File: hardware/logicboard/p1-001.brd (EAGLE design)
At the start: 47 x 72 mm, 24 parts, among them IC1 74LS07N

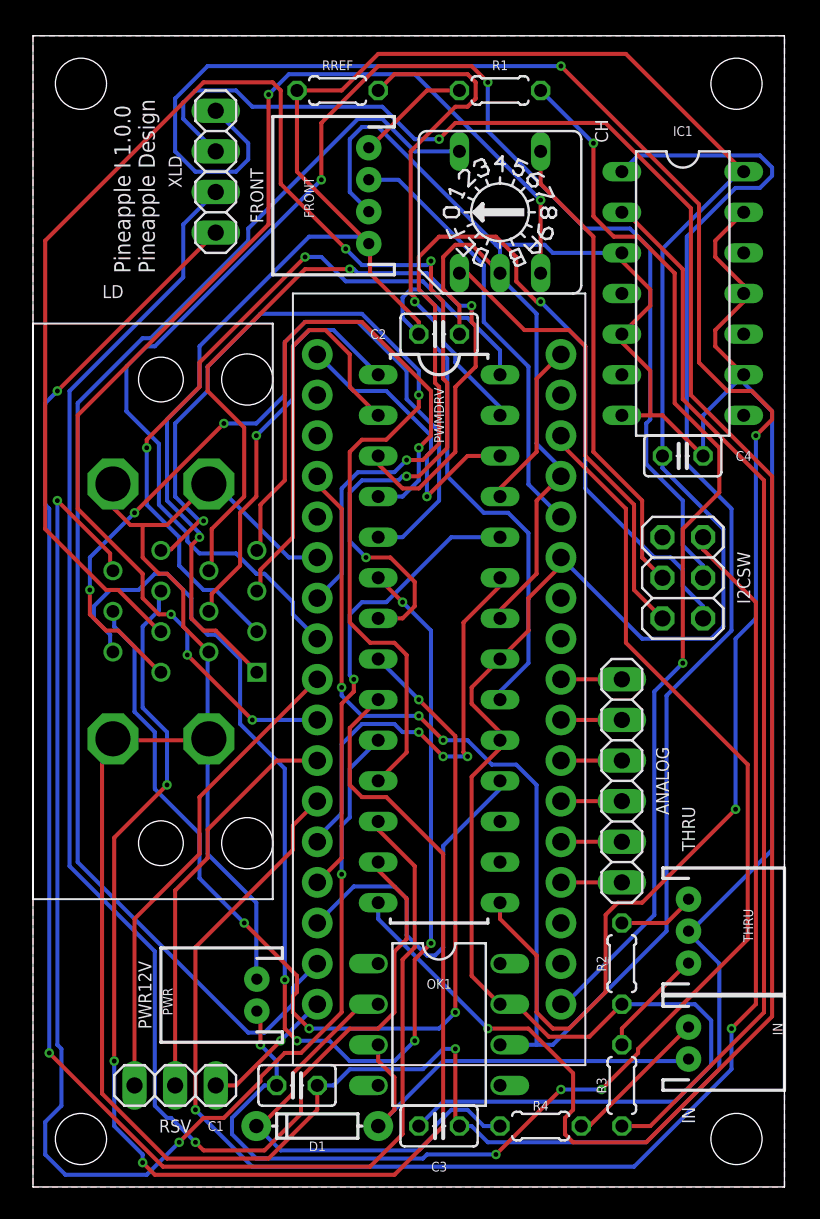
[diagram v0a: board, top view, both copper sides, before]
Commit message: Added MKR compatible I2C connector.
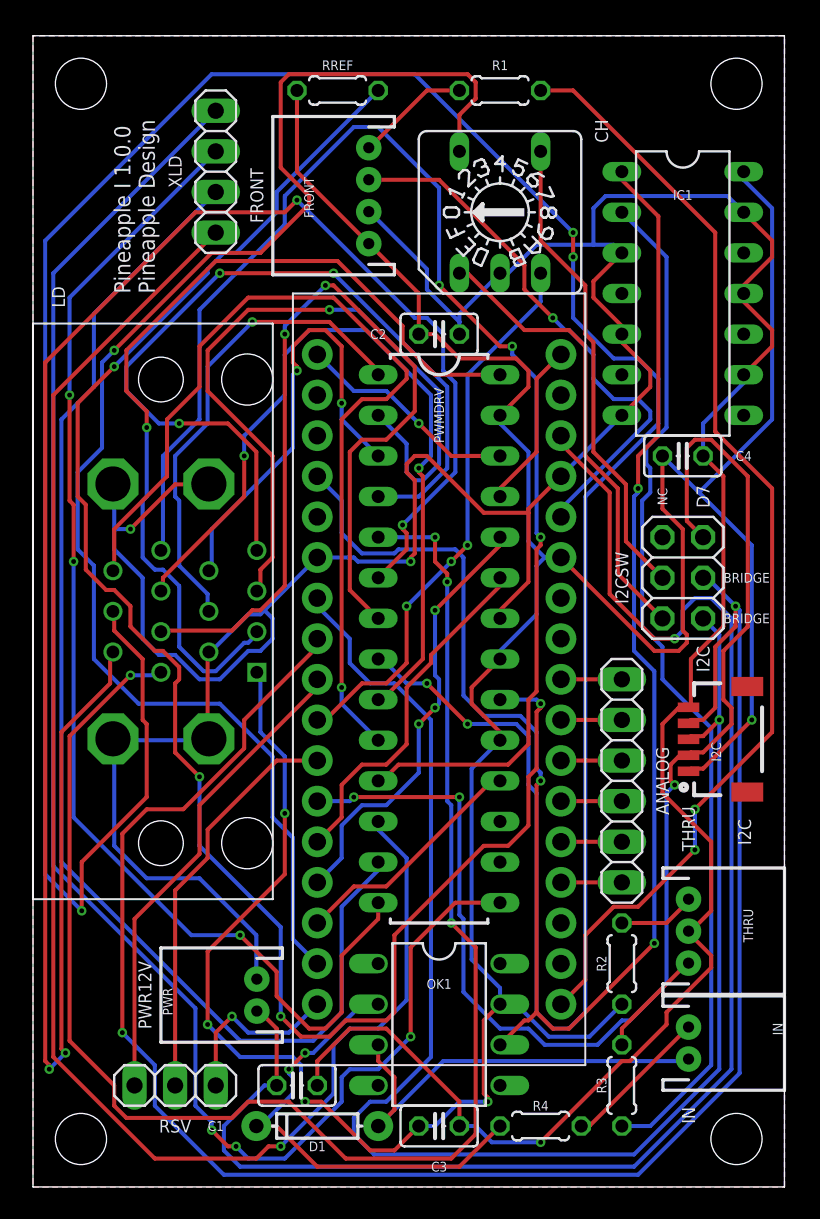
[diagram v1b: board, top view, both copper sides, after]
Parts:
- added I2C: (no value), SparkFun-Connectors:1X05_1MM_RA
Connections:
- net N$11 renamed SW1
- net N$12 renamed SW2
- net N$14 renamed SW4
- net N$15 renamed SW8
- removed net N$10: I2CSW.3, U$1.P$10
- removed net N$13: I2CSW.5, U$1.P$6
- removed net N$9: I2CSW.1, U$1.P$11
- new net D7: I2C.2, I2CSW.5, U$1.P$6
- new net SCL: I2C.4, I2CSW.3, U$1.P$10
- new net SDA: I2C.3, I2CSW.1, U$1.P$11
- net GND: now also I2C.5
- net VCC: now also I2C.1
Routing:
- net LD9: track 65.0 -> 192.1 mm, vias 4 -> 5
- net SCL: track 0.00 -> 118.5 mm, vias 0 -> 2
- net SDA: track 0.00 -> 96.6 mm, vias 0 -> 1
- net N$13: track 95.3 -> 0.00 mm, vias 2 -> 0
- net N$10: track 94.9 -> 0.00 mm, vias 2 -> 0
- net D7: track 0.00 -> 83.1 mm, vias 0 -> 3
- net N$9: track 62.3 -> 0.00 mm, vias 2 -> 0
- net IREF: track 52.1 -> 107.1 mm, vias 1 -> 4
- net LD15: track 130.2 -> 76.9 mm, vias 2 -> 3
- net LD6: track 52.3 -> 99.1 mm, vias 3 -> 4
- net SW4: track 78.5 -> 34.9 mm, vias 5 -> 3
- net LD7: track 80.9 -> 122.6 mm, vias 5 -> 4
- net LD8: track 96.1 -> 55.5 mm, vias 4 -> 2
- net LD10: track 90.0 -> 50.3 mm, vias 3 -> 2
- net LD11: track 88.7 -> 59.0 mm, vias 3 -> 1
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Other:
- board text added: "BRIDGE"
- board text added: "D7"
- board text added: "I2C"
- board text added: "NC"

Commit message: Layout.
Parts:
- turned I2CSW to 270 degrees
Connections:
- net SCL: now also I2C.3; no longer I2C.4
- net SDA: now also I2C.4; no longer I2C.3
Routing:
- net LD9: track 192.1 -> 125.7 mm, vias 5 -> 2
- net LD7: track 122.6 -> 57.7 mm, vias 4 -> 3
- net IREF: track 107.1 -> 47.0 mm, vias 4 -> 0
- net LD6: track 99.1 -> 47.7 mm, vias 4 -> 0
- net SCL: track 118.5 -> 72.4 mm, vias 2 -> 4
- net GND: track 248.9 -> 219.1 mm, vias 3 -> 0
- net LD14: track 79.1 -> 52.8 mm, vias 0 -> 2
- net LD16: track 101.6 -> 124.1 mm, vias 3 -> 1
- net LD3: track 46.4 -> 26.8 mm, vias 1 -> 0
- net LD4: track 28.2 -> 47.2 mm, vias 2 -> 5
- net LD1: track 56.2 -> 71.9 mm, vias 1 -> 3
- net VCC: track 206.4 -> 191.3 mm, vias 5 -> 2
- net LD5: track 53.0 -> 39.2 mm, vias 3 -> 5
- net XLAT: track 27.4 -> 38.4 mm, vias 3 -> 1
- net SW2: track 29.8 -> 40.1 mm
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
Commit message: New silk.
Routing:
- net GND: track 219.1 -> 0.00 mm
- net VCC: track 191.3 -> 0.00 mm, vias 2 -> 0
- net LD9: track 125.7 -> 0.00 mm, vias 2 -> 0
- net LD16: track 124.1 -> 0.00 mm, vias 1 -> 0
- net RX: track 111.7 -> 0.00 mm, vias 2 -> 0
- net VDD: track 95.3 -> 0.00 mm, vias 2 -> 0
- net SW8: track 93.7 -> 0.00 mm, vias 1 -> 0
- net LD13: track 93.2 -> 0.00 mm, vias 1 -> 0
- net SDA: track 90.3 -> 0.00 mm, vias 7 -> 0
- net LD15: track 83.7 -> 0.00 mm
- net D7: track 82.1 -> 0.00 mm, vias 3 -> 0
- net LD12: track 78.5 -> 0.00 mm, vias 5 -> 0
- net SCL: track 72.4 -> 0.00 mm, vias 4 -> 0
- net LD1: track 71.9 -> 0.00 mm, vias 3 -> 0
- net LD11: track 67.0 -> 0.00 mm, vias 3 -> 0
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- removed copper zone on layer 1, net GND
- removed copper zone on layer 16, net GND
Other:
- board text added: "USB"

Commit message: new layout.
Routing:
- net GND: track 0.00 -> 260.2 mm, vias 0 -> 1
- net VCC: track 0.00 -> 237.4 mm
- net LD12: track 0.00 -> 163.7 mm, vias 0 -> 1
- net RX: track 0.00 -> 134.9 mm, vias 0 -> 4
- net LD14: track 0.00 -> 113.9 mm, vias 0 -> 2
- net SCL: track 0.00 -> 111.3 mm, vias 0 -> 2
- net LD15: track 0.00 -> 109.3 mm, vias 0 -> 4
- net VDD: track 0.00 -> 97.5 mm, vias 0 -> 2
- net LD13: track 0.00 -> 95.5 mm, vias 0 -> 3
- net LD16: track 0.00 -> 91.8 mm, vias 0 -> 2
- net SW8: track 0.00 -> 91.6 mm, vias 0 -> 2
- net LD7: track 0.00 -> 89.3 mm, vias 0 -> 4
- net IND: track 0.00 -> 74.9 mm, vias 0 -> 2
- net D7: track 0.00 -> 70.3 mm, vias 0 -> 1
- net LD1: track 0.00 -> 69.9 mm, vias 0 -> 4
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- added copper zone on layer 1, net GND
- added copper zone on layer 16, net GND

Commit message: 20 holes.
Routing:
- net LD12: track 163.7 -> 79.5 mm, vias 1 -> 2
- net IREF: track 44.9 -> 109.4 mm
- net RX: track 134.9 -> 87.0 mm
- net SDA: track 56.1 -> 101.1 mm
- net LD13: track 95.5 -> 51.3 mm, vias 3 -> 2
- net VCC: track 237.4 -> 195.9 mm, vias 0 -> 3
- net LD16: track 91.8 -> 128.4 mm, vias 2 -> 1
- net VDD: track 97.5 -> 132.1 mm
- net SCL: track 111.3 -> 137.6 mm
- net SW1: track 24.8 -> 50.1 mm, vias 0 -> 4
- net LD14: track 113.9 -> 138.3 mm, vias 2 -> 0
- net LD8: track 61.9 -> 85.7 mm, vias 3 -> 2
- net GND: track 260.2 -> 237.8 mm, vias 1 -> 2
- net LD15: track 109.3 -> 87.7 mm, vias 4 -> 3
- net SW4: track 55.5 -> 73.3 mm, vias 5 -> 3
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
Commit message: New silk.
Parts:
- added VOUT: (no value), pinhead:1X03
- moved I2CSW 1.27 mm to (41.9, 38.1)
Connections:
- new net 3V: U$1.P$33, VOUT.1, VOUT.2
- net GND: now also VOUT.3
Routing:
- net GND: track 237.8 -> 299.2 mm, vias 2 -> 3
- net LD16: track 128.4 -> 70.2 mm, vias 1 -> 2
- net LD3: track 38.9 -> 77.1 mm, vias 0 -> 9
- net VCC: track 195.9 -> 234.0 mm, vias 3 -> 4
- net RX: track 87.0 -> 125.0 mm, vias 4 -> 3
- net LD14: track 138.3 -> 106.0 mm, vias 0 -> 8
- net LD8: track 85.7 -> 55.8 mm, vias 2 -> 3
- net SCL: track 137.6 -> 107.8 mm, vias 2 -> 3
- net LD12: track 79.5 -> 106.7 mm, vias 2 -> 7
- net 3V: track 0.00 -> 25.7 mm
- net LD4: track 58.5 -> 33.2 mm, vias 1 -> 2
- net LD11: track 64.1 -> 87.0 mm, vias 2 -> 3
- net LD9: track 59.7 -> 82.4 mm, vias 1 -> 7
- net SDA: track 101.1 -> 120.7 mm
- net LD6: track 77.9 -> 58.8 mm, vias 2 -> 5
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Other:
- board text added: "G"
- board text removed: "BRIDGE"

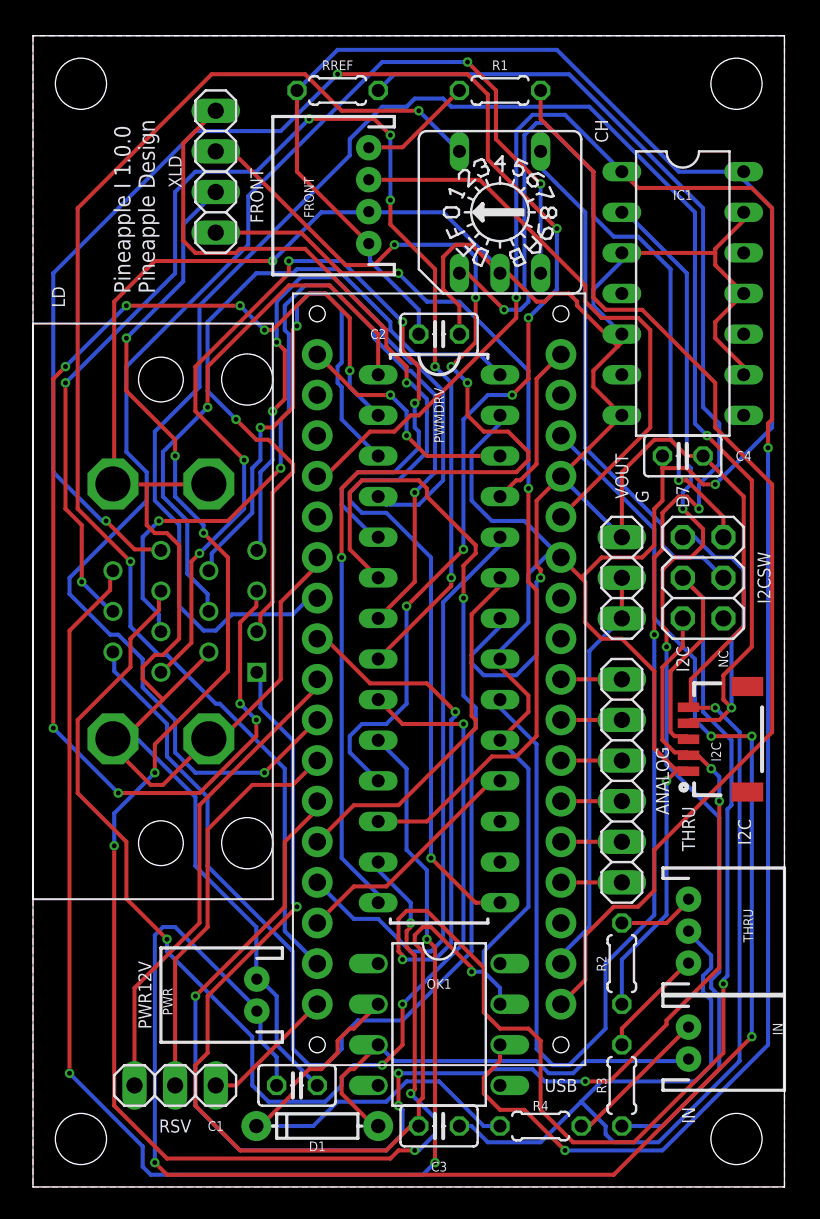
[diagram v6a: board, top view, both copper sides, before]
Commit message: Vcc and Vref terminal.
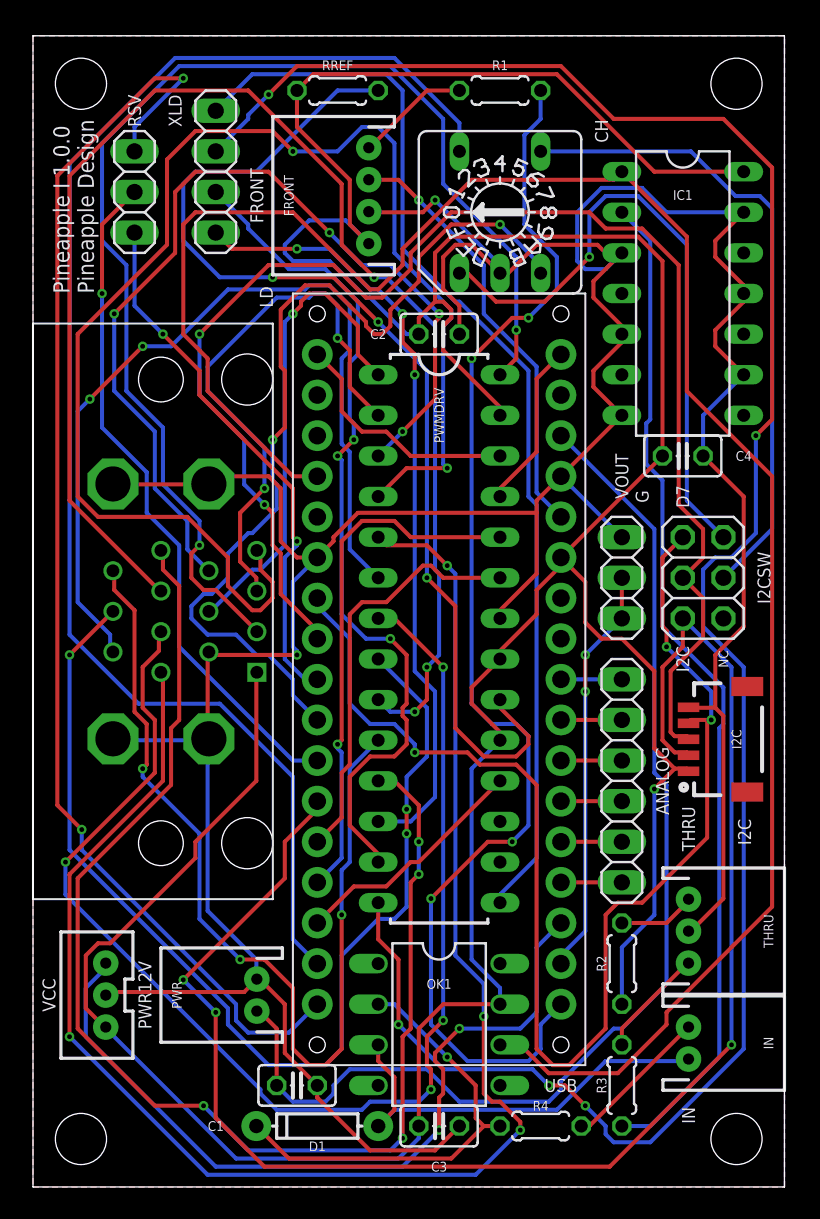
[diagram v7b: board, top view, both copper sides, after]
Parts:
- added VCC: (no value), SparkFun-Connectors:JST-3-PTH-VERT
- moved RSV 55.9 mm to (6.35, 62.2), turned to 90 degrees
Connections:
- new net VREF: U$1.P$32, VCC.3
- net GND: now also VCC.2
- net VCC: now also VCC.1
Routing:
- net RSV3: track 8.45 -> 79.8 mm, vias 0 -> 2
- net GND: track 299.2 -> 238.0 mm, vias 3 -> 2
- net LD15: track 75.5 -> 133.8 mm
- net LD14: track 106.0 -> 53.7 mm, vias 8 -> 3
- net VREF: track 0.00 -> 50.4 mm, vias 0 -> 2
- net LD5: track 41.4 -> 87.0 mm
- net LD3: track 77.1 -> 34.8 mm, vias 9 -> 2
- net LD6: track 58.8 -> 100.7 mm, vias 5 -> 4
- net VDD: track 113.6 -> 72.4 mm, vias 4 -> 0
- net IREF: track 109.2 -> 69.0 mm, vias 2 -> 3
- net SDA: track 120.7 -> 81.6 mm, vias 2 -> 3
- net LD1: track 45.7 -> 78.4 mm, vias 1 -> 2
- net LD7: track 86.8 -> 55.0 mm, vias 1 -> 2
- net SW4: track 86.6 -> 57.8 mm, vias 3 -> 2
- net LD11: track 87.0 -> 59.8 mm
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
